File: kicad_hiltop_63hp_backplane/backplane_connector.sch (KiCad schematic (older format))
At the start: 49 parts, among them J4 CONN_DIN_HDR_96POS, J5 CONN_DIN_HDR_96POS, J6 CONN_DIN_HDR_96POS, U3 LTC4311, U4 LTC4311

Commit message: routing on differential, USB, Power and internconnects
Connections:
- net labels added: LVPSCLK-
- net labels removed: LVDSCLK-
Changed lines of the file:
@@
 LVPSCLK+
 Text HLabel 900  6100 3    39   Input ~ 0
-LVDSCLK-
+LVPSCLK-
 Wire Wire Line
 	4825 5950 4725 5950
@@
 LVPSCLK+
 Text HLabel 4425 6100 3    39   Input ~ 0
-LVDSCLK-
+LVPSCLK-
 Wire Wire Line
 	4425 5950 4425 5900
@@
 LVPSCLK+
 Text HLabel 7950 6100 3    39   Input ~ 0
-LVDSCLK-
+LVPSCLK-
 Wire Wire Line
 	7950 5950 7950 5900

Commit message: Rev A
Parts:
- C20, C21: symbol device:C -> hiltop_backplane_brd-rescue:C-device; Devtank (none) -> 105-017
- F1, F11, F12, F13, F2, F3, F6, F7, F8: symbol device:Polyfuse -> hiltop_backplane_brd-rescue:Polyfuse-device; Devtank (none) -> 190-002
- F10, F15, F5: symbol device:Polyfuse -> hiltop_backplane_brd-rescue:Polyfuse-device; Devtank (none) -> 190-004
- F14, F4, F9: symbol device:Polyfuse -> hiltop_backplane_brd-rescue:Polyfuse-device; Devtank (none) -> 190-003
- J4, J5, J6: symbol gti_Lattice:CONN_DIN_HDR_96POS -> hiltop_backplane_brd-rescue:CONN_DIN_HDR_96POS-gti_Lattice; Devtank (none) -> 717-001
- R18, R20, R21, R23, R24, R26, R27, R29, R30, R32, R33, R35, R36, R38, R39, R41, R42, R44: symbol device:R -> hiltop_backplane_brd-rescue:R-device; Devtank (none) -> 101-510
- R19, R22, R25, R28, R31, R34, R37, R40, R43: symbol device:R -> hiltop_backplane_brd-rescue:R-device; Devtank (none) -> 101-500
- U3, U4: symbol gti_Lattice:LTC4311 -> hiltop_backplane_brd-rescue:LTC4311-gti_Lattice; Devtank (none) -> 118-010

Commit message: add latest changes
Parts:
- C20, C21: symbol hiltop_backplane_brd-rescue:C-device -> hiltop_backplane_brd-rescue:C-device-hiltop_backplane_brd-rescue
- F1, F10, F11, F12, F13, F14, F15, F2, F3, F4, F5, F6, F7, F8, F9: symbol hiltop_backplane_brd-rescue:Polyfuse-device -> hiltop_backplane_brd-rescue:Polyfuse-device-hiltop_backplane_brd-rescue
- J4, J5, J6: symbol hiltop_backplane_brd-rescue:CONN_DIN_HDR_96POS-gti_Lattice -> hiltop_backplane_brd-rescue:CONN_DIN_HDR_96POS-gti_Lattice-hiltop_backplane_brd-rescue
- R18, R19, R20, R21, R22, R23, R24, R25, R26, R27, R28, R29, R30, R31, R32, R33, R34, R35, R36, R37, R38, R39, R40, R41, R42, R43, R44: symbol hiltop_backplane_brd-rescue:R-device -> hiltop_backplane_brd-rescue:R-device-hiltop_backplane_brd-rescue
- U3, U4: symbol hiltop_backplane_brd-rescue:LTC4311-gti_Lattice -> hiltop_backplane_brd-rescue:LTC4311-gti_Lattice-hiltop_backplane_brd-rescue

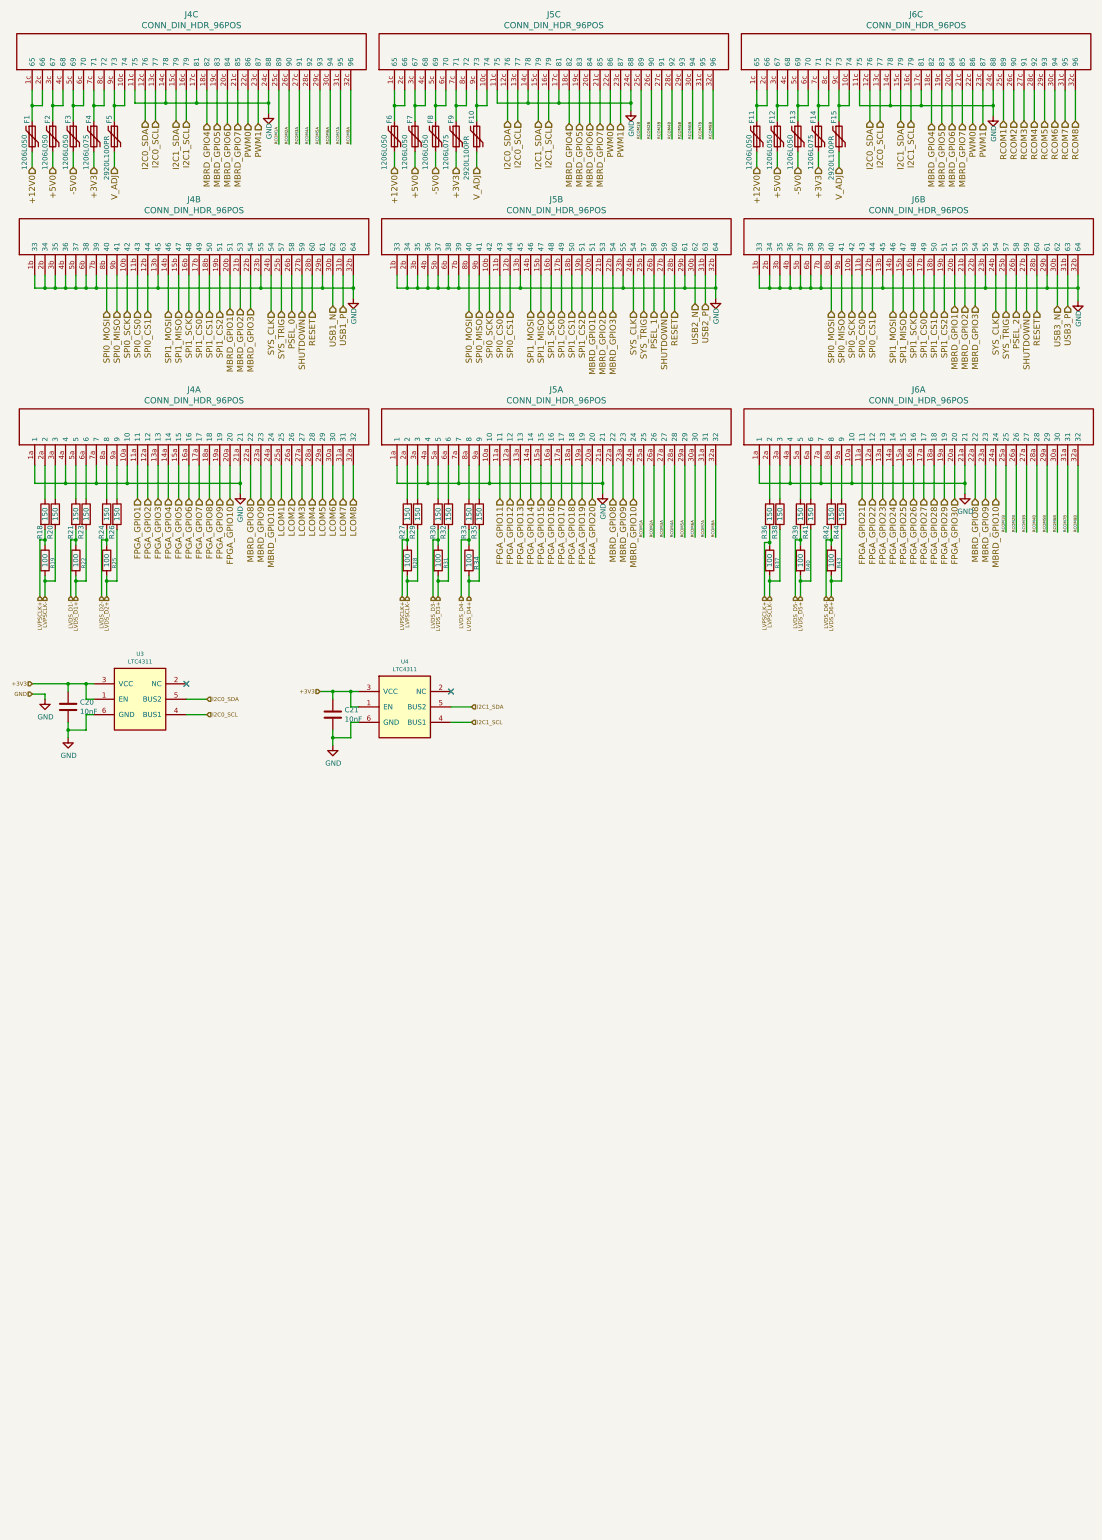
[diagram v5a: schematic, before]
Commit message: updated schematics to RevC including general tidy up
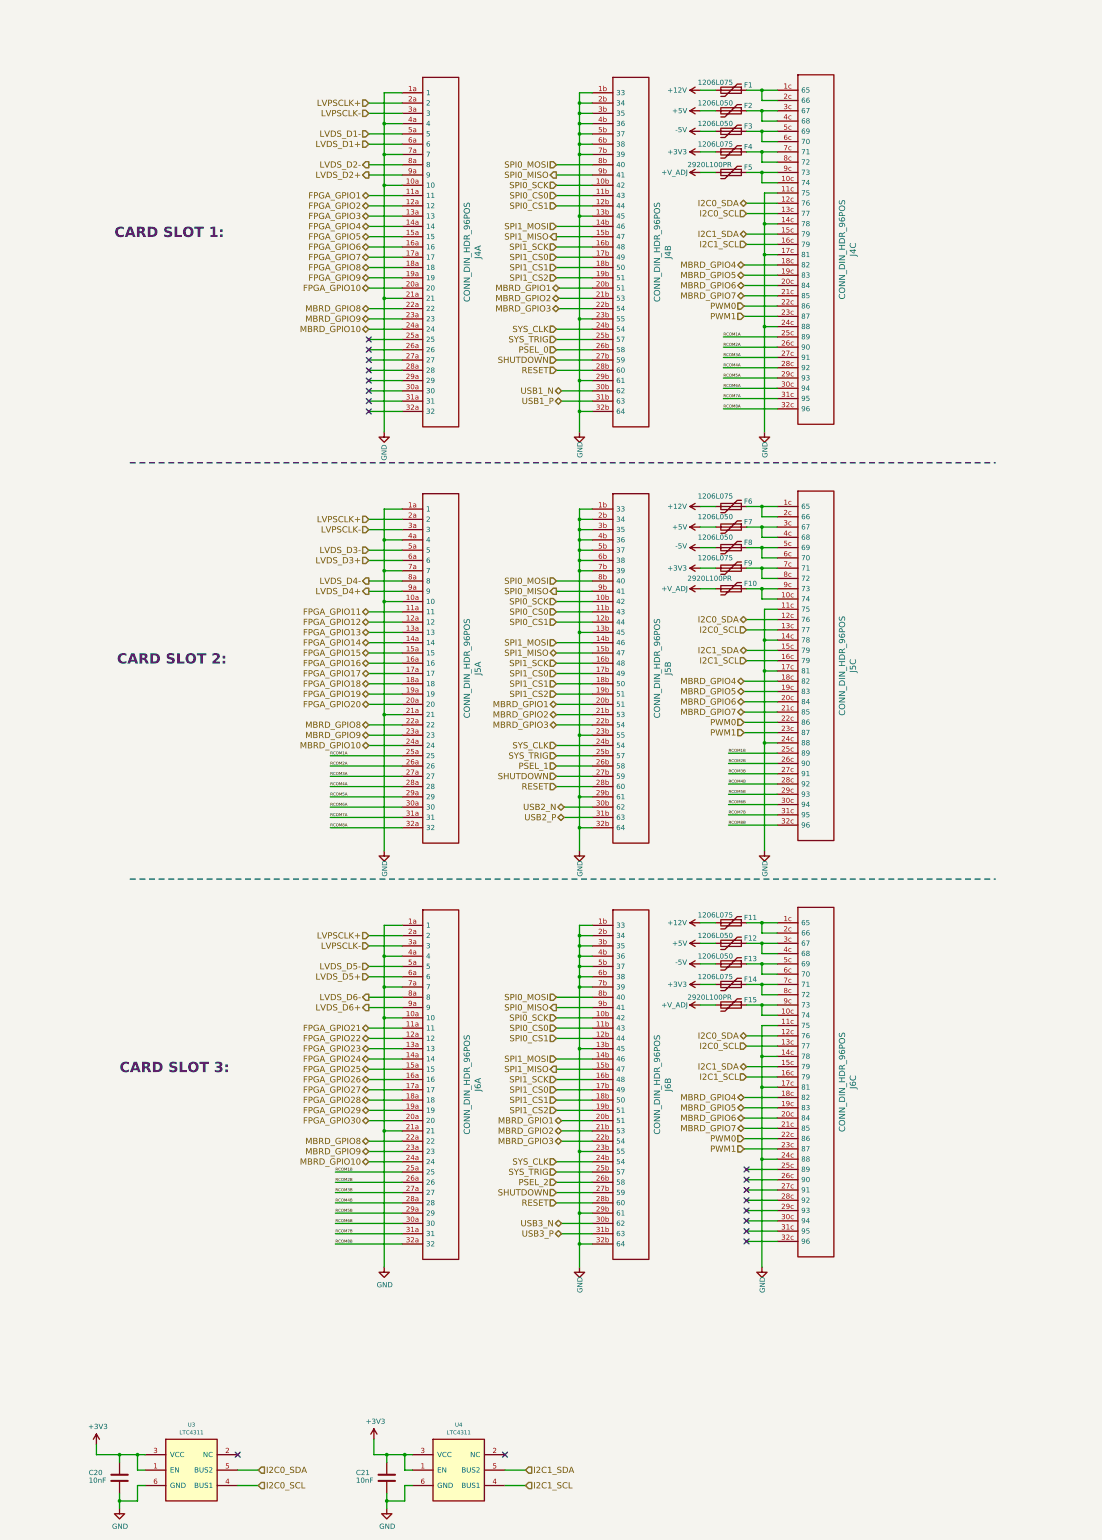
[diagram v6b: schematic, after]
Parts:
- removed R18, R20, R21, R23, R24, R26, R27, R29, R30, R32, R33, R35, R36, R38, R39, R41, R42, R44: 150, Resistor_SMD:R_0402_1005Metric, symbol hiltop_backplane_brd-rescue:R-device-hiltop_backplane_brd-rescue
- removed R19, R22, R25, R28, R31, R34, R37, R40, R43: 100, Resistor_SMD:R_0402_1005Metric, symbol hiltop_backplane_brd-rescue:R-device-hiltop_backplane_brd-rescue
- F1, F11, F6: value 1206L050 -> 1206L075
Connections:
- net LVDS_D1+: now also J4.6a (6)
- net LVDS_D1-: now also J4.5a (5)
- net LVDS_D2+: now also J4.9a (9)
- net LVDS_D2-: now also J4.8a (8)
- net LVDS_D3+: now also J5.6a (6)
- net LVDS_D3-: now also J5.5a (5)
- net LVDS_D4+: now also J5.9a (9)
- net LVDS_D4-: now also J5.8a (8)
- net LVDS_D5+: now also J6.6a (6)
- net LVDS_D5-: now also J6.5a (5)
- net LVDS_D6+: now also J6.9a (9)
- net LVDS_D6-: now also J6.8a (8)
- net LVPSCLK+: now also J4.2a (2), J5.2a (2), J6.2a (2)
- net LVPSCLK-: now also J4.3a (3), J5.3a (3), J6.3a (3)
- net +12V0 renamed +12V
- net +5V0 renamed +5V
- net -5V0 renamed -5V
- net LCOM1: no longer names the net of J4.25a (25)
- net LCOM2: no longer names the net of J4.26a (26)
- net LCOM3: no longer names the net of J4.27a (27)
- net LCOM4: no longer names the net of J4.28a (28)
- net LCOM5: no longer names the net of J4.29a (29)
- net LCOM6: no longer names the net of J4.30a (30)
- net LCOM7: no longer names the net of J4.31a (31)
- net LCOM8: no longer names the net of J4.32a (32)
- net RCOM1: no longer names the net of J6.25c (89)
- net RCOM2: no longer names the net of J6.26c (90)
- net RCOM3: no longer names the net of J6.27c (91)
- net RCOM4: no longer names the net of J6.28c (92)
- net RCOM5: no longer names the net of J6.29c (93)
- net RCOM6: no longer names the net of J6.30c (94)
- net RCOM7: no longer names the net of J6.31c (95)
- net RCOM8: no longer names the net of J6.32c (96)
- net V_ADJ renamed +V_ADJ
- no-connect marks 2 -> 18
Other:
- note added: "CARD SLOT 1:"
- note added: "CARD SLOT 2:"
- note added: "CARD SLOT 3:"
- moved on the sheet: C20, C21, F1, F10, F11, F12, F13, F14, F15, F2, F3, F4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
